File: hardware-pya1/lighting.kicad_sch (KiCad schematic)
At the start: 25 parts

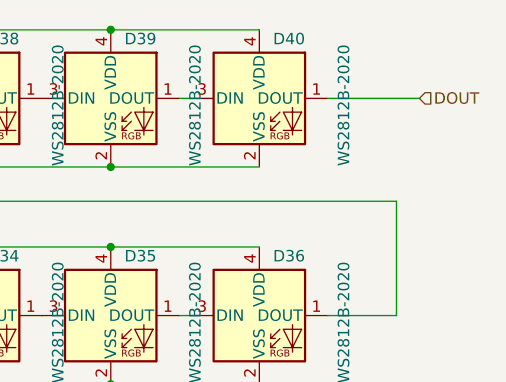
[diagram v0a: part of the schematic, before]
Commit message: pcb: redesign fix for LowPowerReq - added passives optional cap for slowstart on regulator switching to hi-power
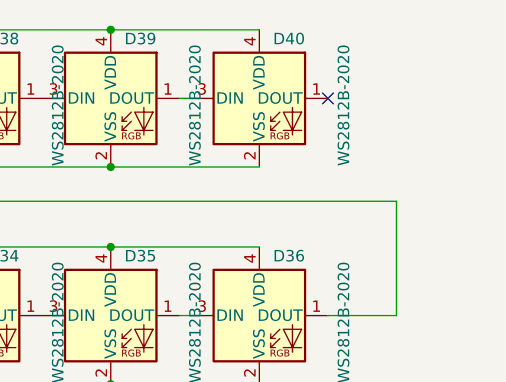
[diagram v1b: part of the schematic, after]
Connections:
- net DOUT: no longer names the net of D40.1 (DOUT)
- no-connect marks 0 -> 1
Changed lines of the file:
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@@
 		(color 0 0 0 0)
 	)
+	(no_connect
+		(at 175.26 49.53)
+	)
 	(wire
 		(pts
@@
 		(pts
 			(xy 120.65 113.03) (xy 135.89 113.03)
-		)
-		(stroke
-			(width 0)
-			(type default)
-		)
-	)
-	(wire
-		(pts
-			(xy 185.42 49.53) (xy 175.26 49.53)
 		)
 		(stroke
@@
 		)
 	)
-	(hierarchical_label "DOUT"
-		(shape input)
-		(at 185.42 49.53 0)
-		(effects
-			(font
-				(size 1.27 1.27)
-			)
-			(justify left)
-		)
-	)
